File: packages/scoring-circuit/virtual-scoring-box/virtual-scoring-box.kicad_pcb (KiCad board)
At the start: 4 copper layers, 120 x 85 mm, 90 parts, among them J2 STM SWD 3.3V, J3 LEFT WEAPON A B C, J4 RIGHT WEAPON A B C, J5 PISTE - NOT protective earth, J6 ESP 3.3V UART recovery, SW1 STM RESET, SW2 ESP RESET, SW3 ESP BOOT, U1 STM32G474RET6, U10 SN74AXC1T45DCKR, U11 SN74AXC1T45DCKR, U13 TSOP38438, U2 ESP32-S3-WROOM-1-N8R8, U8 74LVC125APW, U9 74LVC125APW, Y1 ABM3B-8.000MHZ-B2-T

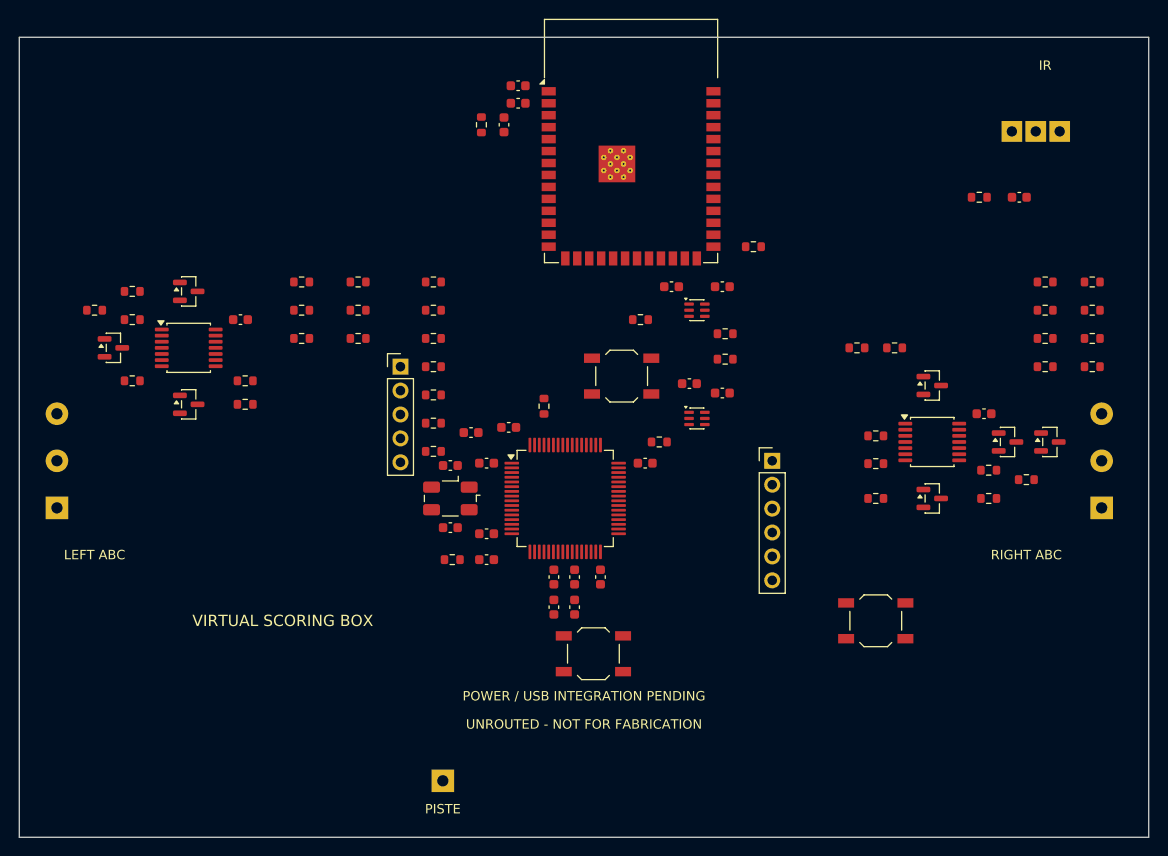
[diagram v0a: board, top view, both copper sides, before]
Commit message: feat(scoring-circuit): add virtual box USB interface and signal routing checkpoint
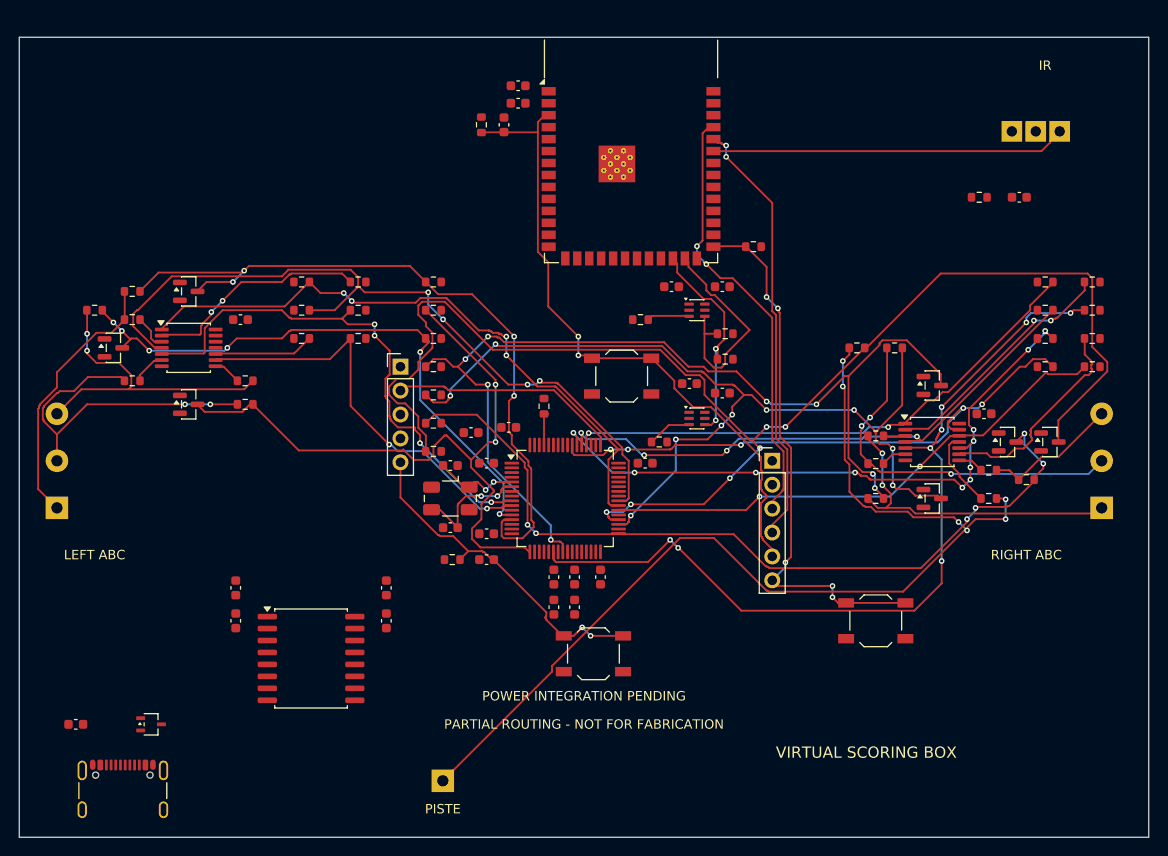
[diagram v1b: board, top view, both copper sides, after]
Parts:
- added C1: 1uF 50V, Capacitor_SMD:C_0603_1608Metric, F.Cu at (56.0, 123.0)
- added C35: 1uF, Capacitor_SMD:C_0603_1608Metric, F.Cu at (73.0, 108.5)
- added C36: 100nF, Capacitor_SMD:C_0603_1608Metric, F.Cu at (73.0, 112.0)
- added C37: 1uF, Capacitor_SMD:C_0603_1608Metric, F.Cu at (89.0, 108.5)
- added C38: 100nF, Capacitor_SMD:C_0603_1608Metric, F.Cu at (89.0, 112.0)
- added J1: GCT USB4105-GF-A, ScoringPlatform:USB4105_GF_A, F.Cu at (61.0, 131.0)
- added U18: ISOUSB111DWR, Package_SO:SOIC-16W_7.5x10.3mm_P1.27mm, F.Cu at (81.0, 116.0)
- added U3: TPD2E2U06DCKR, ScoringPlatform:TPD2E2U06DCKR, F.Cu at (64.0, 123.0)
- U2: footprint RF_Module:ESP32-S3-WROOM-1 -> ScoringPlatform:ESP32-S3-WROOM-1_Edge
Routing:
- net PISTE_SENSE: track 0.00 -> 149.6 mm, vias 0 -> 6
- net PISTE: track 0.00 -> 109.7 mm, vias 0 -> 6
- net RIGHT_A_SENSE: track 0.00 -> 106.0 mm, vias 0 -> 8
- net RIGHT_B_SENSE: track 0.00 -> 99.7 mm, vias 0 -> 10
- net RIGHT_B_DRIVE: track 0.00 -> 89.5 mm, vias 0 -> 8
- net RIGHT_C_SENSE: track 0.00 -> 86.9 mm, vias 0 -> 6
- net LEFT_B_OE_N: track 0.00 -> 81.9 mm, vias 0 -> 4
- net LEFT_A_SENSE: track 0.00 -> 78.2 mm, vias 0 -> 4
- net LEFT_B_SENSE: track 0.00 -> 72.6 mm, vias 0 -> 2
- net ESP_EN: track 0.00 -> 70.2 mm, vias 0 -> 2
- net RIGHT_C_OE_N: track 0.00 -> 68.8 mm, vias 0 -> 11
- net LEFT_A_OE_N: track 0.00 -> 67.0 mm, vias 0 -> 4
- net LEFT_C_SENSE: track 0.00 -> 63.2 mm, vias 0 -> 6
- net PISTE_OE_N: track 0.00 -> 61.1 mm, vias 0 -> 5
- net RIGHT_B_OE_N: track 0.00 -> 61.0 mm, vias 0 -> 4
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- added copper zone on In1.Cu, net GND
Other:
- board text added: "PARTIAL ROUTING - NOT FOR FABRICATION"
- board text added: "POWER INTEGRATION PENDING"
- board text removed: "POWER / USB INTEGRATION PENDING"
- board text removed: "UNROUTED - NOT FOR FABRICATION"

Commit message: feat(scoring-circuit): connect virtual box ground pads to inner plane
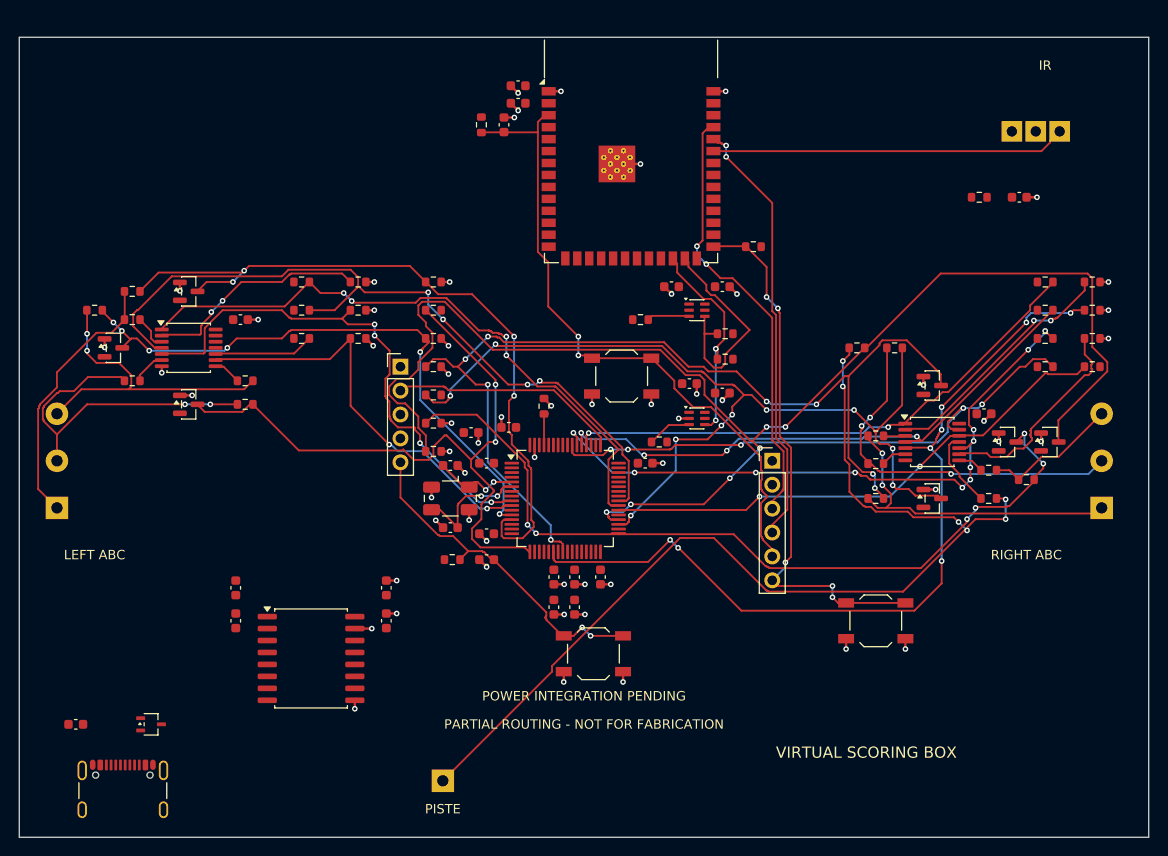
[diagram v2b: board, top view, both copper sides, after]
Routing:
- net GND: track 0.00 -> 65.0 mm, vias 0 -> 59

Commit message: feat(scoring-circuit): add suspend-aware isolated serial interface
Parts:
- added C39: 1uF, Capacitor_SMD:C_0603_1608Metric, F.Cu at (54.5, 111.0)
- added C40: 1uF, Capacitor_SMD:C_0603_1608Metric, F.Cu at (62.5, 111.0)
- added R74: 1k, Resistor_SMD:R_0603_1608Metric, F.Cu at (62.0, 116.0)
- added R75: 10k, Resistor_SMD:R_0603_1608Metric, F.Cu at (71.0, 118.5)
- added R76: 22.1k, Resistor_SMD:R_0603_1608Metric, F.Cu at (59.0, 119.0)
- added R77: 47.5k, Resistor_SMD:R_0603_1608Metric, F.Cu at (59.0, 121.0)
- added R78: 10k, Resistor_SMD:R_0603_1608Metric, F.Cu at (90.0, 118.0)
- added U19: ISO7021DR, Package_SO:SOIC-8_3.9x4.9mm_P1.27mm, F.Cu at (83.0, 116.0)
- added U20: TLV75533PDBVR, Package_TO_SOT_SMD:SOT-23-5, F.Cu at (59.0, 111.0)
- C1: value 1uF 50V -> 1uF
- C35: value 1uF -> 4.7uF
- C37: value 1uF -> 100nF
- U18: value ISOUSB111DWR -> CP2102N-A02-GQFN20R; footprint Package_SO:SOIC-16W_7.5x10.3mm_P1.27mm -> ScoringPlatform:CP2102N_QFN20
- moved U18 14.5 mm to (66.5, 117.0)
- moved C37 12.7 mm to (77.5, 114.0)
- moved C35 8.54 mm to (65.0, 111.5), turned to 0 degrees
- moved C36 7.16 mm to (66.0, 113.5), turned to 0 degrees
- moved C38 2.06 mm to (88.5, 114.0)
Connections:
- C37 pad 1: CORE_3V3 -> USB_HOST_3V3
- C37 pad 2: GND -> USB_GND
- U1 pad 14: unconnected-(U1-PA2-Pad14) -> LAPTOP_UART_TX
- U1 pad 45: USB_DM -> unconnected-(U1-PA11-Pad45)
- U1 pad 46: USB_DP -> unconnected-(U1-PA12-Pad46)
- U1 pad 51: unconnected-(U1-PA15-Pad51) -> LAPTOP_UART_RX
- U1 pad 58: USB_PRESENT -> unconnected-(U1-PB5-Pad58)
- U18 pad 1: USB_HOST_3V3 -> unconnected-(U18-RS485/GPIO.1-Pad1)
- U18 pad 10: USB_DP -> unconnected-(U18-NC-Pad10)
- U18 pad 11: USB_DM -> USB_AWAKE
- U18 pad 12: CORE_3V3 -> USB_GND
- U18 pad 13: unconnected-(U18-NC-Pad13) -> USB_HOST_3V3
- U18 pad 14: CORE_3V3 -> unconnected-(U18-SUSPEND-Pad14)
- U18 pad 15: GND -> USB_GND
- U18 pad 16: CORE_3V3 -> unconnected-(U18-~{RTS}-Pad16)
- U18 pad 2: USB_GND -> unconnected-(U18-CLK/GPIO.0-Pad2)
- U18 pad 3: USB_HOST_3V3 -> USB_GND
- U18 pad 4: unconnected-(U18-NC-Pad4) -> USB_HOST_DP
- U18 pad 5: unconnected-(U18-NC-Pad5) -> USB_HOST_DM
- U18 pad 6: USB_HOST_DM -> USB_HOST_3V3
- U18 pad 7: USB_HOST_DP -> USB_HOST_3V3
- U18 pad 8: USB_GND -> USB_VBUS_SENSE
- U18 pad 9: GND -> USB_BRIDGE_RESET_N
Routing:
- net GND: track 65.0 -> 60.1 mm, vias 59 -> 55

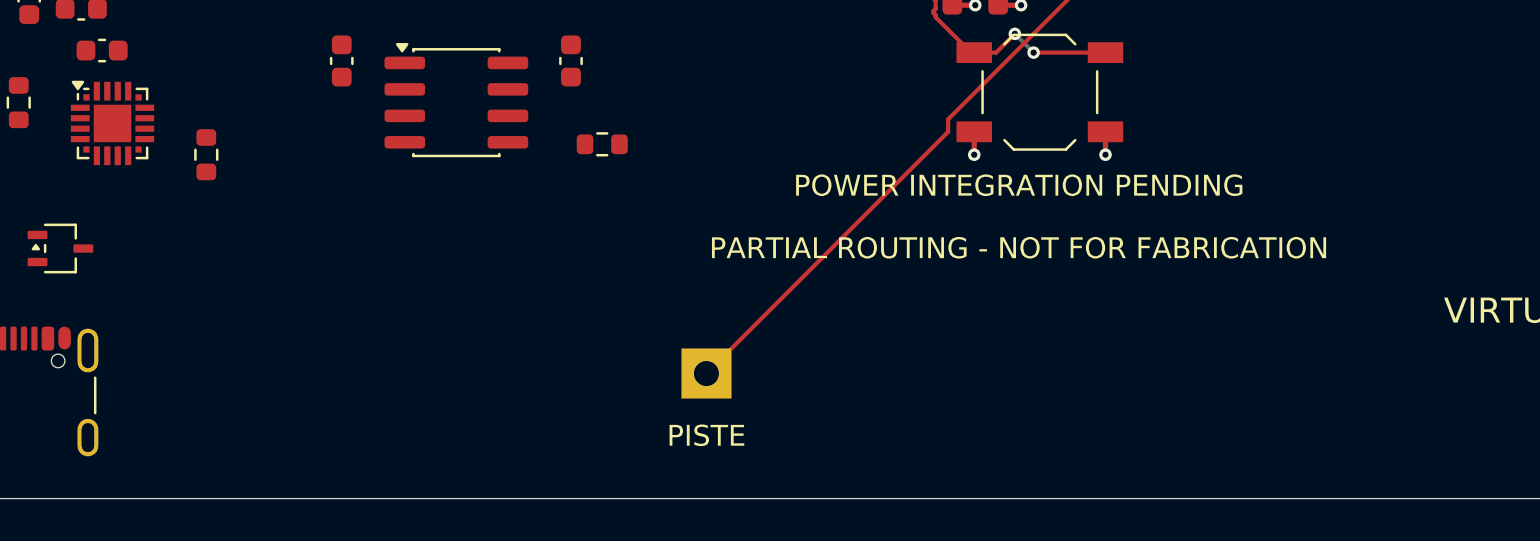
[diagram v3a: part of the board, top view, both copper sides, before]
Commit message: feat(scoring-circuit): integrate isolated virtual-box processor supply
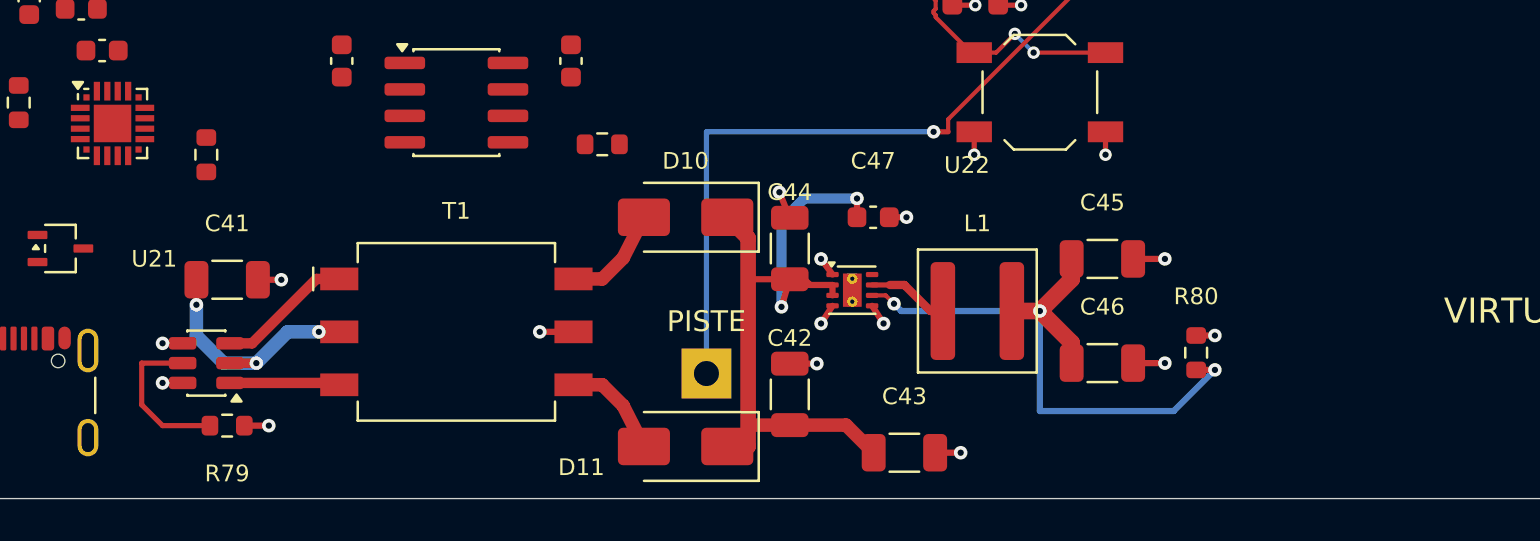
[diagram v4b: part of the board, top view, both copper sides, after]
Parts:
- added C41: 10uF 16V X7R, Capacitor_SMD:C_1206_3216Metric, F.Cu at (72.0, 124.5)
- added C42: 10uF 16V X7R, Capacitor_SMD:C_1206_3216Metric, F.Cu at (99.0, 130.0)
- added C43: 10uF 16V X7R, Capacitor_SMD:C_1206_3216Metric, F.Cu at (104.5, 132.8)
- added C44: 10uF 16V X7R, Capacitor_SMD:C_1206_3216Metric, F.Cu at (99.0, 123.0)
- added C45: 10uF 16V X7R, Capacitor_SMD:C_1206_3216Metric, F.Cu at (114.0, 123.5)
- added C46: 10uF 16V X7R, Capacitor_SMD:C_1206_3216Metric, F.Cu at (114.0, 128.5)
- added C47: 100nF, Capacitor_SMD:C_0603_1608Metric, F.Cu at (103.0, 121.5)
- added D10: SS14-E3/61T, Diode_SMD:D_SMA, F.Cu at (94.0, 121.5)
- added D11: SS14-E3/61T, Diode_SMD:D_SMA, F.Cu at (94.0, 132.5)
- added L1: 2.2uH, Inductor_SMD:L_Coilcraft_XAL5030-XXX, F.Cu at (108.0, 126.0)
- added R79: 100k, Resistor_SMD:R_0603_1608Metric, F.Cu at (72.0, 131.5)
- added R80: 10k, Resistor_SMD:R_0603_1608Metric, F.Cu at (118.5, 128.0)
- added T1: 750315371, ScoringPlatform:750315371, F.Cu at (83.0, 127.0)
- added U21: SN6505BDBVR, Package_TO_SOT_SMD:SOT-23-6, F.Cu at (71.0, 128.5)
- added U22: TPS62162DSGR, Package_SON:Texas_DSG0008A_WSON-8-1EP_2x2mm_P0.5mm_EP0.9x1.6mm_ThermalVias, F.Cu at (102.0, 125.0)
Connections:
- C22 pad 1: APP_3V3 -> CORE_3V3
- C23 pad 1: APP_3V3 -> CORE_3V3
- C25 pad 1: APP_3V3 -> CORE_3V3
- C27 pad 1: APP_3V3 -> CORE_3V3
- J6 pad 1: APP_3V3 -> CORE_3V3
- R28 pad 1: APP_3V3 -> CORE_3V3
- R29 pad 1: APP_3V3 -> CORE_3V3
- R31 pad 1: APP_3V3 -> CORE_3V3
- R32 pad 1: APP_3V3 -> CORE_3V3
- R73 pad 1: APP_3V3 -> CORE_3V3
- U10 pad 6: APP_3V3 -> CORE_3V3
- U11 pad 6: APP_3V3 -> CORE_3V3
- U2 pad 2: APP_3V3 -> CORE_3V3
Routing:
- net ISO_UNREG: track 0.00 -> 34.1 mm, vias 0 -> 2
- net CORE_3V3: track 0.00 -> 30.9 mm, vias 0 -> 3
- net GND: track 60.1 -> 73.3 mm, vias 55 -> 66
- net USB_5V_PROTECTED: track 0.00 -> 12.0 mm, vias 0 -> 3
- net SCORING_POWER_EN: track 0.00 -> 7.65 mm
- net PISTE: track 109.7 -> 116.5 mm, vias 6 -> 7
- net XFMR_PRI_B: track 0.00 -> 6.52 mm
- net XFMR_PRI_A: track 0.00 -> 5.25 mm
- net XFMR_SEC_B: track 0.00 -> 4.99 mm
- net XFMR_SEC_A: track 0.00 -> 4.99 mm
- net USB_GND: track 0.00 -> 4.22 mm, vias 0 -> 4
- net CORE_BUCK_SW: track 0.00 -> 3.91 mm
- added copper zone on In2.Cu, net USB_GND
